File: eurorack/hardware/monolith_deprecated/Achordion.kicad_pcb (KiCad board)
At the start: 4 copper layers, 44.5 x 109.4 mm, 120 parts, among them J1 Power, J10 Jack, J11 Jack, J2 Serial, J3 SWD, J4 Jack, J5 Jack, J6 Jack, J7 Jack, J8 Jack, J9 Jack, SW2 Button, U1 STM32F405RGT6, U10 SC39-11SURKWA, U2 LM1117-3.3, U3 LM1117-3.3, U4 LM4040C10, U5 TLV320AIC23BPW, U6 TL072, U7 MCP6002, U8 MCP6002, U9 MCP6002, Y1 8MHz

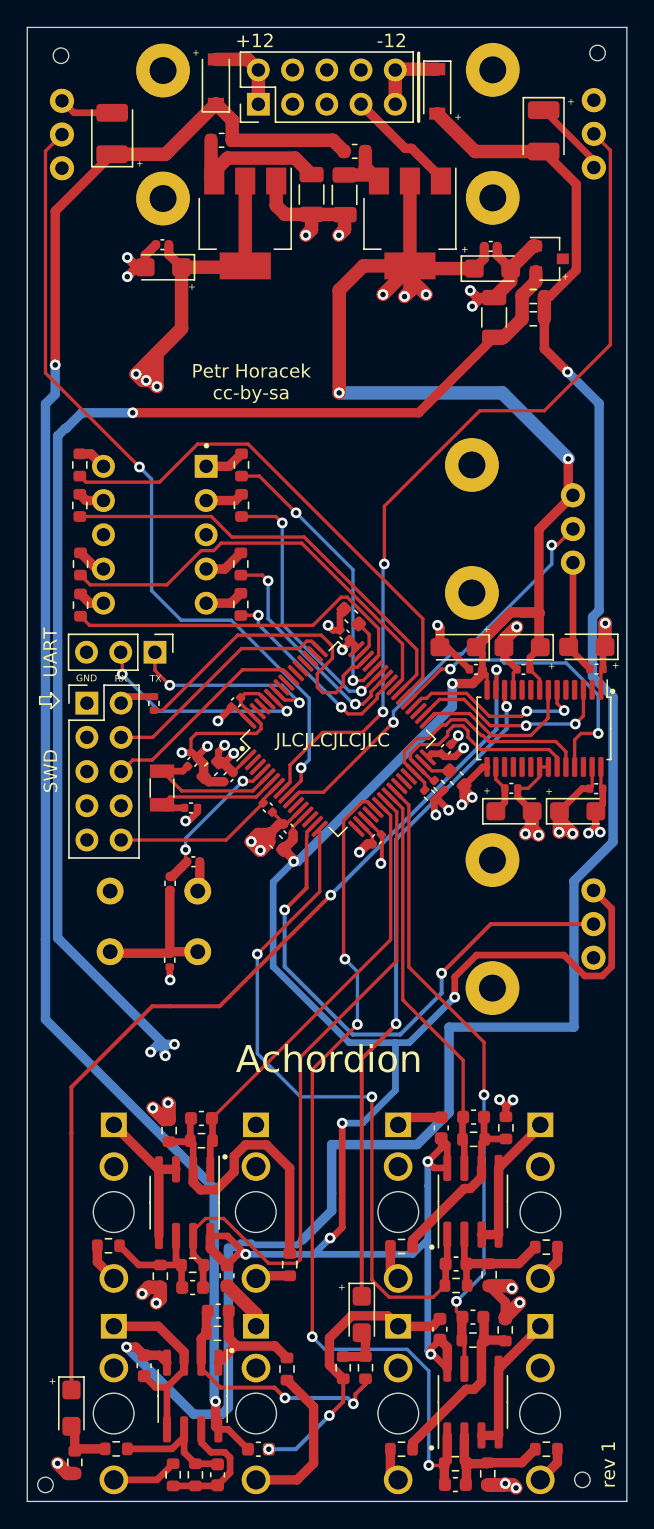
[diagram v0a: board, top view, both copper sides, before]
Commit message: Move harware to its own directory
JLCPCB does not offer the MCU this was designed for. I'm starting again,
this time making the design modular.

Signed-off-by: Petr Horacek <hrck@protonmail.com>
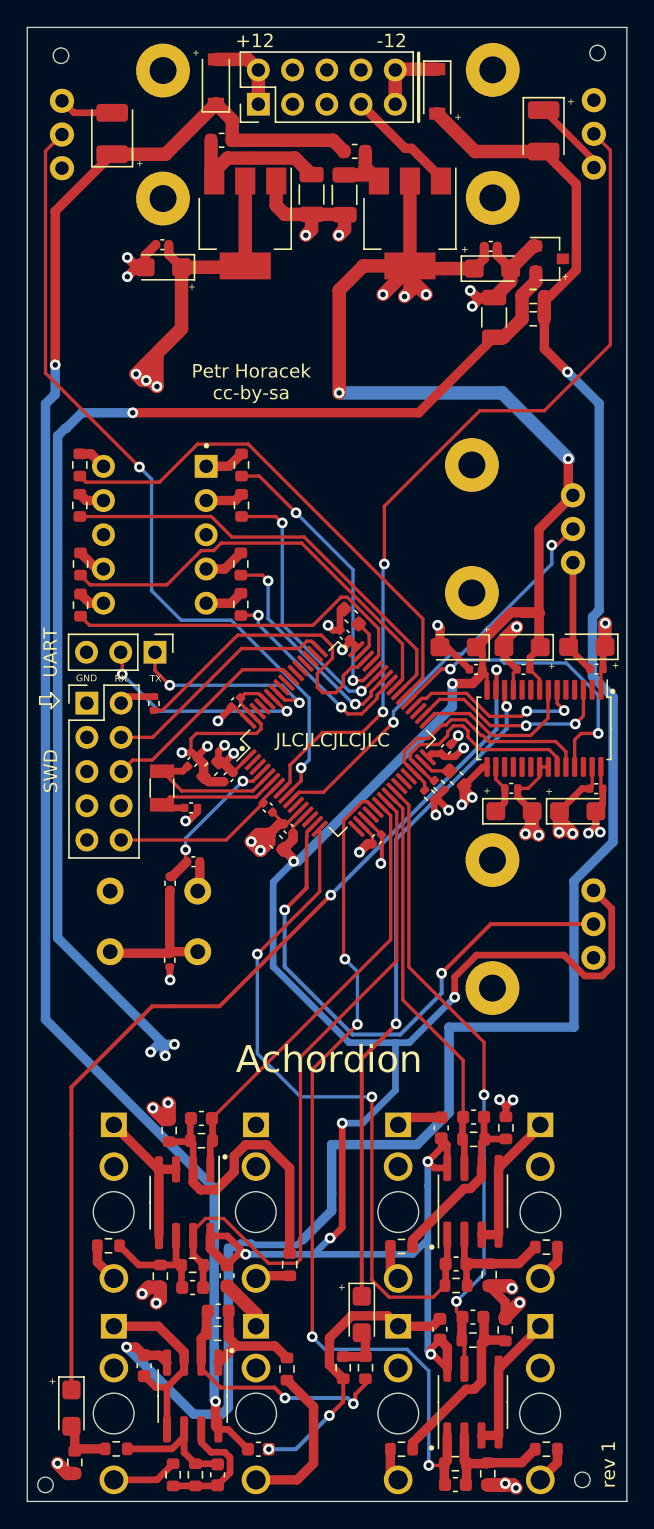
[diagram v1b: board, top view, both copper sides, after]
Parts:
- R16: value 160 -> 10k
